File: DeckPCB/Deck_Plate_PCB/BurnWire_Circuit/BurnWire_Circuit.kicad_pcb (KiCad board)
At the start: 2 copper layers, 8 parts, among them J1 Board_to_Board, Q1 BurnWire

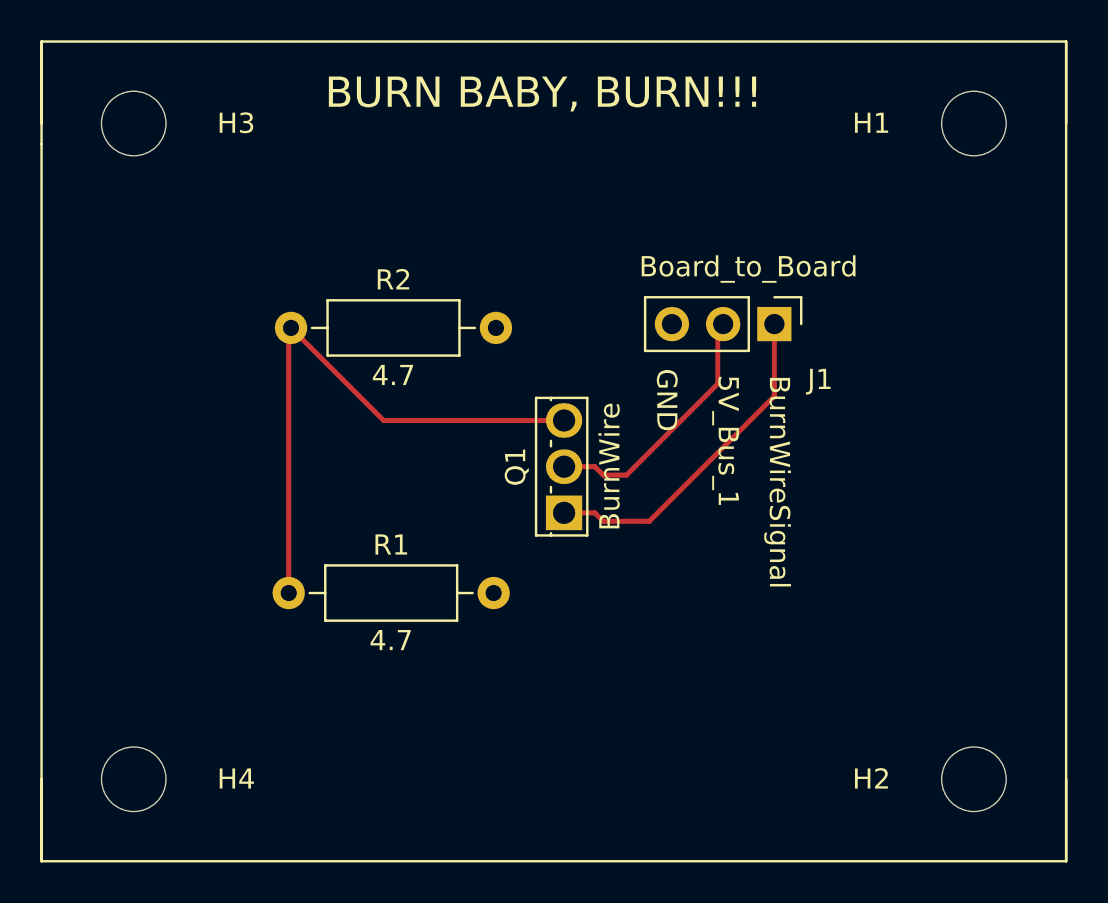
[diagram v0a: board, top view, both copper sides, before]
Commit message: updated PCB routing and creation of BurnWire circuit board and updated Daughter_Board
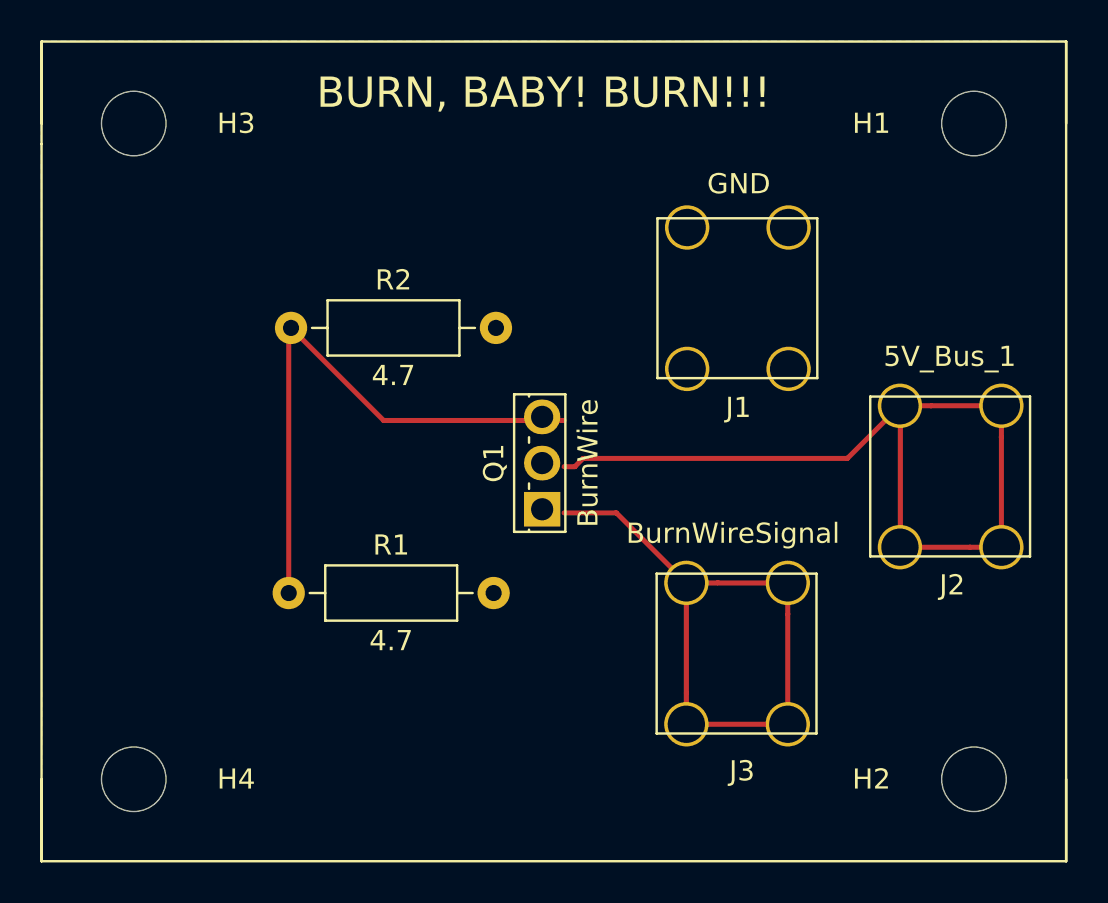
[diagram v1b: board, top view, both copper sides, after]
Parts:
- added J2: 5V_Bus_1, Deck_Plate_PCB:Terminal_Lug_PCB, F.Cu at (210.2, 81.0)
- added J3: BurnWireSignal, Deck_Plate_PCB:Terminal_Lug_PCB, F.Cu at (199.6, 89.7)
- J1: value Board_to_Board -> GND; footprint Connector_PinHeader_2.54mm:PinHeader_1x03_P2.54mm_Vertical -> Deck_Plate_PCB:Terminal_Lug_PCB
- moved J1 4.86 mm to (199.7, 72.1), turned to 0 degrees
- moved Q1 1.10 mm to (192.5, 79.1)
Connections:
- J1 pad 1: /BurnWireSignal -> GND
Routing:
- net /5V_Bus_1: track 12.8 -> 42.0 mm
- net /BurnWireSignal: track 16.7 -> 31.6 mm
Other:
- board text added: "BURN, BABY! BURN!!!"
- board text removed: "5V_Bus_1"
- board text removed: "BURN BABY, BURN!!!"
- board text removed: "BurnWireSignal"
- board text removed: "GND"

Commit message: Updated Main_Deck_Plate and Daughter_Board to fit Electronics Enclosure internal dimensions. Created all PCB Gerber files. Created all PCB PNG images. Created all PCB STEP files for mechanical integration. Implemented all design review comments and corrections.
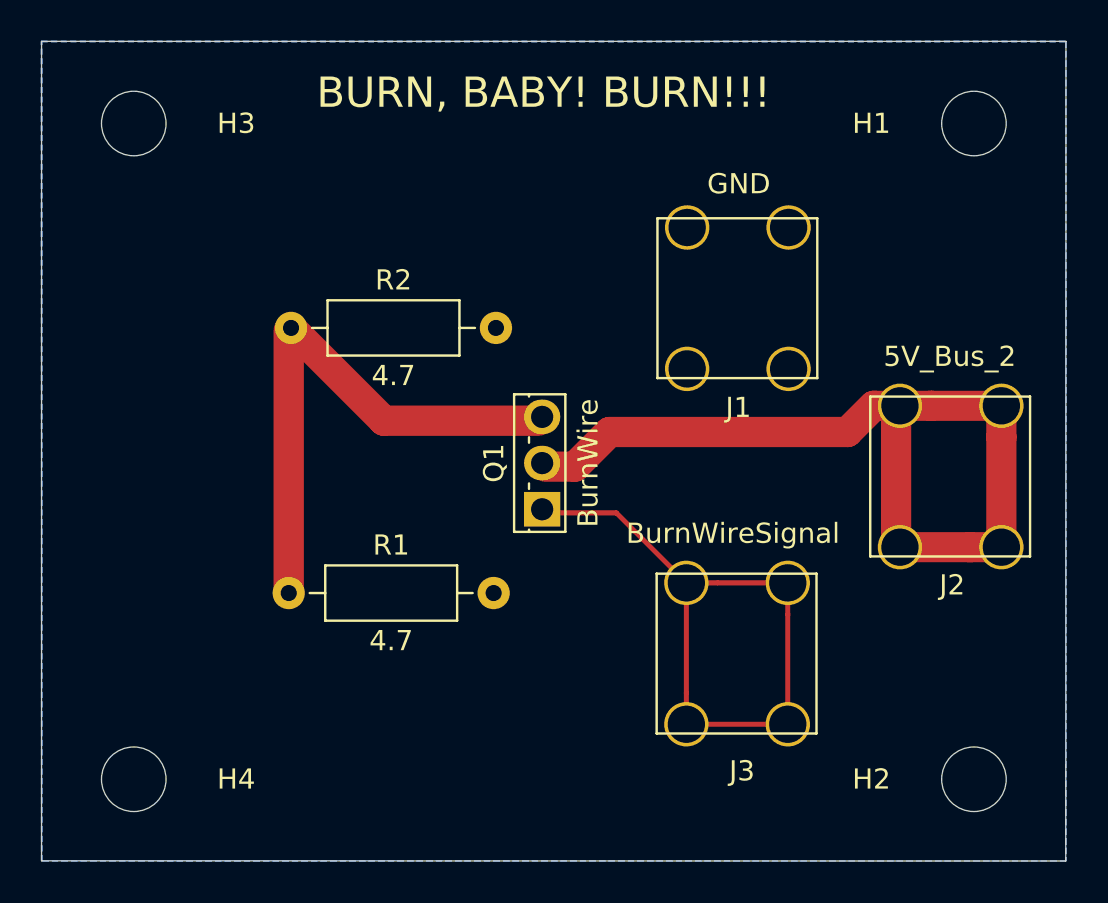
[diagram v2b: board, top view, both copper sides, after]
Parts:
- J2: value 5V_Bus_1 -> 5V_Bus_2
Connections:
- net /5V_Bus_1 renamed /5V_Bus_2
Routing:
- net /5V_Bus_2: track 42.0 -> 43.3 mm
- net /BurnWireSignal: track 31.6 -> 32.7 mm
- net Net-(Q1-Pad3): track 28.6 -> 27.6 mm
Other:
- board outline added: 50.8 x 40.6 mm
